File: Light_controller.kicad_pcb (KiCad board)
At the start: 2 copper layers, 11 parts, among them U1 LM358DR, U2 PT8211-S, U3 STM8S003F3P, U4 LTV-356T, U5 LTV-356T

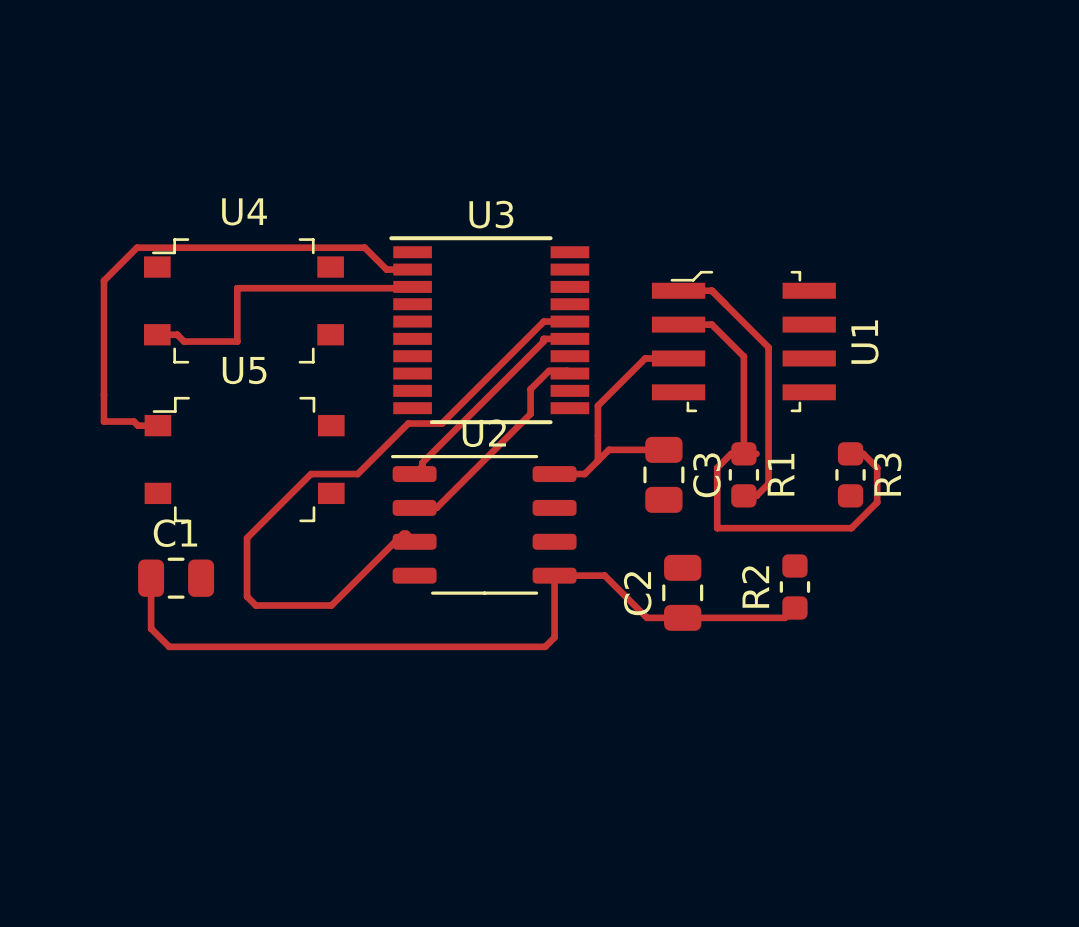
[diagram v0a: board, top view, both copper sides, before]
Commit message: added all circuit except temperature sensor
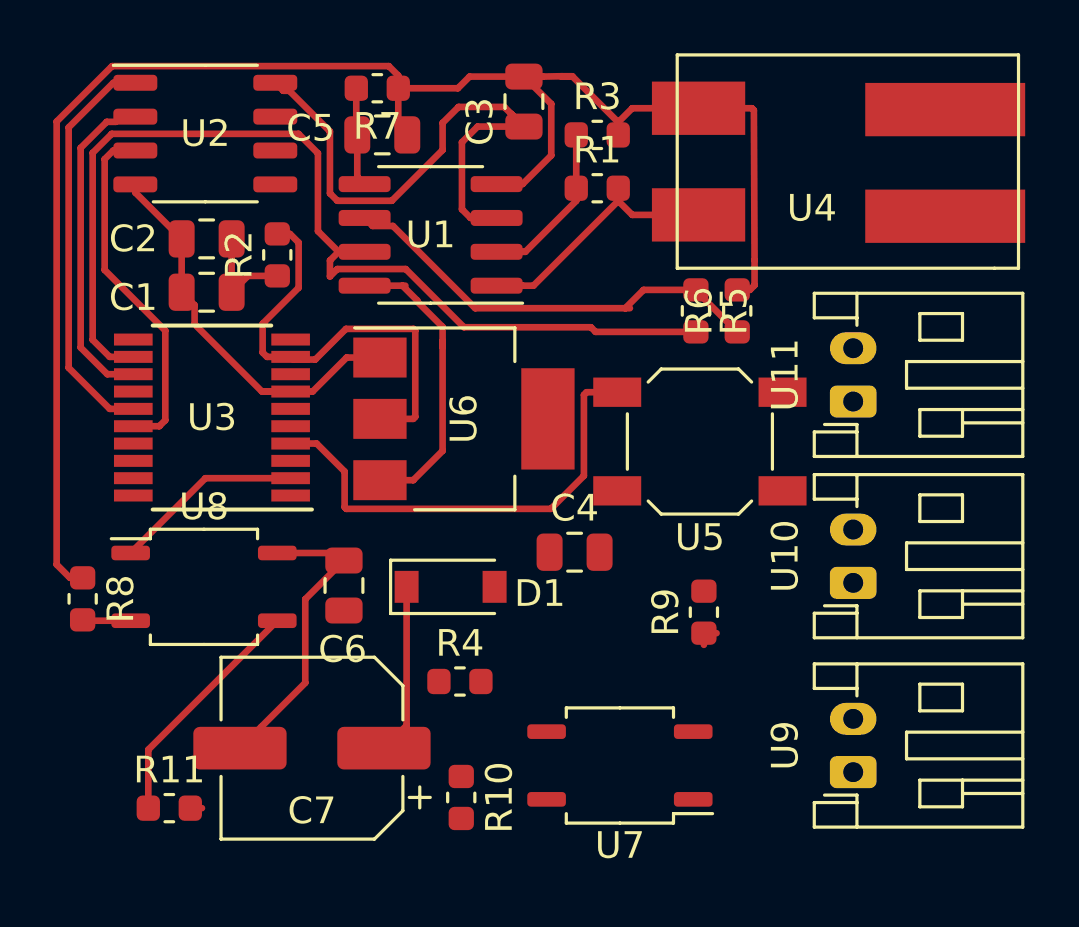
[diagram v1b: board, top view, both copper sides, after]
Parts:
- added C4: C, Capacitor_SMD:C_0805_2012Metric, F.Cu at (170.7, 70.9)
- added C5: C, Capacitor_SMD:C_0805_2012Metric, F.Cu at (163.4, 55.2)
- added C6: C, Capacitor_SMD:C_0805_2012Metric, F.Cu at (162.0, 72.2)
- added C7: 470uF, Capacitor_SMD:CP_Elec_6.3x7.7, F.Cu at (160.8, 78.2)
- added D1: 1N5819HW, Diode_SMD:D_SOD-123, F.Cu at (166.0, 72.2)
- added R10: R, Resistor_SMD:R_0603_1608Metric, F.Cu at (166.4, 80.1)
- added R11: 1K, Resistor_SMD:R_0603_1608Metric, F.Cu at (155.4, 80.5)
- added R4: R, Resistor_SMD:R_0603_1608Metric, F.Cu at (166.3, 75.8)
- added R5: R, Resistor_SMD:R_0603_1608Metric, F.Cu at (175.2, 61.9)
- added R6: R, Resistor_SMD:R_0603_1608Metric, F.Cu at (176.8, 61.9)
- added R7: 0.01Ω, Resistor_SMD:R_0603_1608Metric, F.Cu at (163.2, 53.5)
- added R8: R, Resistor_SMD:R_0603_1608Metric, F.Cu at (152.2, 72.7)
- added R9: R, Resistor_SMD:R_0603_1608Metric, F.Cu at (175.5, 73.2)
- added U10: PH2.0_horizontal, Connector_JST:JST_PH_S2B-PH-K_1x02_P2.00mm_Horizontal, F.Cu at (181.1, 72.0)
- added U11: PH2.0_horizontal, Connector_JST:JST_PH_S2B-PH-K_1x02_P2.00mm_Horizontal, F.Cu at (181.1, 65.2)
- added U6: AMS1117-5.0, Package_TO_SOT_SMD:SOT-223, F.Cu at (166.5, 65.9)
- added U7: EL357N-C, Package_SO:SOP-4_3.8x4.1mm_P2.54mm, F.Cu at (172.3, 78.9)
- added U8: EL357N-C, Package_SO:SOP-4_3.8x4.1mm_P2.54mm, F.Cu at (156.8, 72.2)
- added U9: PH2.0_horizontal, Connector_JST:JST_PH_S2B-PH-K_1x02_P2.00mm_Horizontal, F.Cu at (181.1, 79.2)
- R1, R2, R3: footprint Capacitor_SMD:C_0603_1608Metric -> Resistor_SMD:R_0603_1608Metric
- U1: value LM358DR -> LM358; footprint digikey-footprints:SOIC-8_W3.9mm -> Package_SO:SOIC-8_3.9x4.9mm_P1.27mm
- U4: value LTV-356T -> SMD_2062; footprint digikey-footprints:SMD-4_4.4x3.85mm_P2.54mm -> Custom_footprint_lib:LEDSMD2062
- U5: value LTV-356T -> tact_sw; footprint digikey-footprints:SMD-4_4.4x3.85mm_P2.54mm -> Button_Switch_SMD:SW_SPST_SKQG_WithStem
- moved U4 24.3 mm to (182.5, 62.2), turned to 180 degrees
- moved R2 23.1 mm to (159.5, 59.8)
- moved C2 22.2 mm to (156.8, 59.1), turned to 180 degrees
- moved U2 18.0 mm to (156.8, 55.2)
- moved U5 17.1 mm to (175.3, 66.8), turned to 180 degrees
- moved R3 15.9 mm to (171.5, 55.2), turned to 0 degrees
- moved C3 15.0 mm to (168.8, 54.0), turned to 90 degrees
- moved U1 12.4 mm to (165.2, 59.0), turned to 180 degrees
- moved R1 12.1 mm to (171.5, 57.2), turned to 0 degrees
- moved U3 11.0 mm to (157.1, 65.8), turned to 180 degrees
- moved C1 10.8 mm to (156.8, 61.1), turned to 180 degrees
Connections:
- net Net-(U3-Pad10) renamed /PA3
- net Net-(U3-Pad11) renamed /PB5
- net Net-(U3-Pad14) renamed /PC4
- net Net-(U3-Pad17) renamed /PC7
- net Net-(U3-Pad19) renamed /PD2
- net Net-(U3-Pad20) renamed /V_SENSOR
- net Net-(U3-Pad5) renamed /PA1
- net Net-(U3-Pad6) renamed /PA2
- net Net-(U3-Pad8) renamed /VCAP
- U1 pad 5: (no net) -> /CURRENT_IN
- U1 pad 6: (no net) -> Net-(R5-Pad1)
- U1 pad 7: (no net) -> /C_SENSOR
- U2 pad 6: (no net) -> Net-(U2-Pad6)
- U3 pad 12: Net-(U3-Pad12) -> /C_SENSOR
- U3 pad 4: /SWIM_RST -> /RESET
- U3 pad 9: Net-(U3-Pad9) -> /5V_SUPPLY
- U4 pad 1: Net-(U4-Pad1) -> Net-(R1-Pad2)
- U4 pad 2: /UART_RX -> GND
- U5 pad 1: /UART_TX -> GND
- U5 pad 2: GND -> /RESET
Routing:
- net GND: track 0.00 -> 78.5 mm
- net /C_SENSOR: track 0.00 -> 39.2 mm
- net Net-(C1-Pad1): track 29.6 -> 3.97 mm
- net /RESET: track 0.00 -> 17.6 mm
- net /5V_SUPPLY: track 0.00 -> 16.8 mm
- net Net-(R5-Pad1): track 0.00 -> 16.5 mm
- net Net-(R1-Pad1): track 19.5 -> 6.25 mm
- net /UART_TX: track 19.8 -> 7.16 mm
- net /SPI_MOSI: track 25.3 -> 13.3 mm
- net /RCH: track 10.3 -> 22.1 mm
- net +12V: track 0.00 -> 11.4 mm
- net Net-(C6-Pad1): track 0.00 -> 11.3 mm
- net /UART_RX: track 11.7 -> 0.91 mm
- net Net-(R11-Pad1): track 0.00 -> 9.03 mm
- net /SPI_SCK: track 8.05 -> 15.3 mm
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
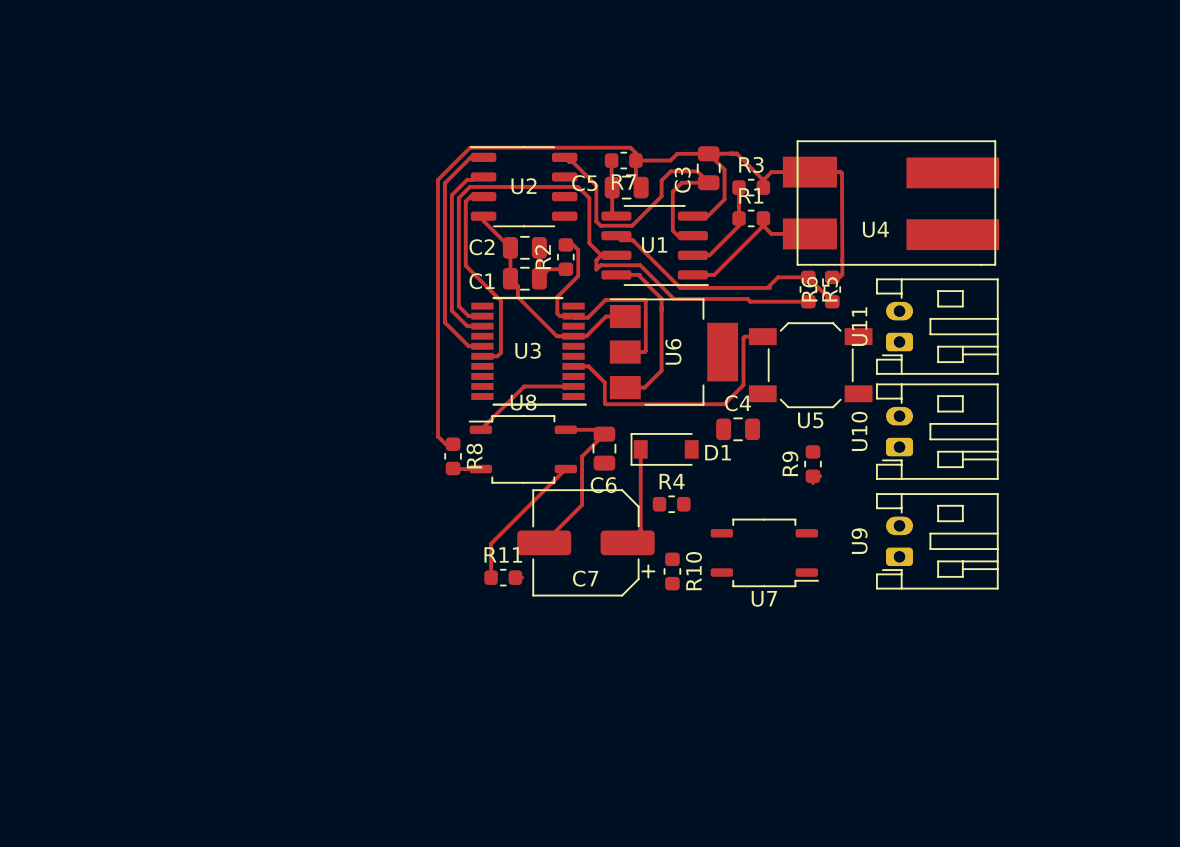
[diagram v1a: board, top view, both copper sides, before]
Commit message: modified ph2.0 to smd , changed thermistor to a ph2.0 and rerouted the layout again with via
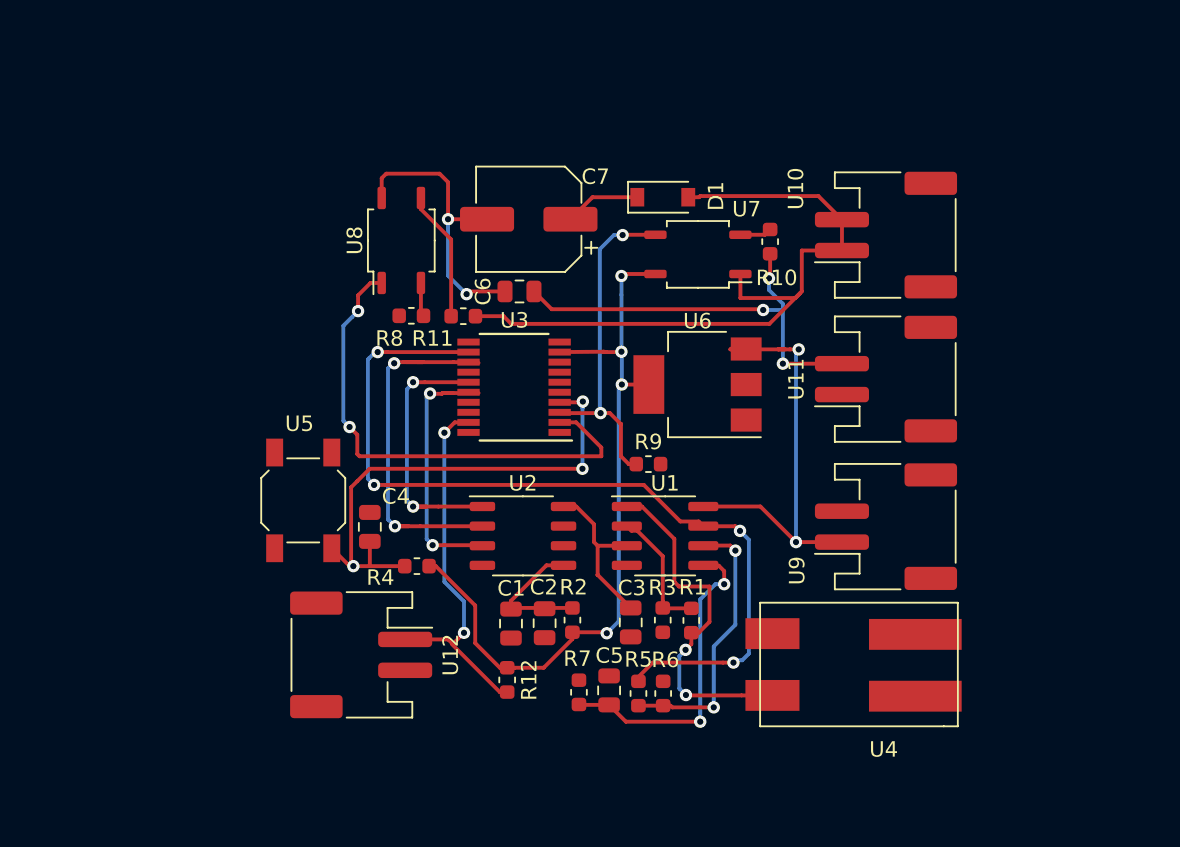
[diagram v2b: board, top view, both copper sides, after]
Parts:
- added R12: R, Resistor_SMD:R_0603_1608Metric, F.Cu at (155.7, 87.1)
- added U12: PH2.0_horizontal, Connector_JST:JST_PH_S2B-PH-SM4-TB_1x02-1MP_P2.00mm_Horizontal, F.Cu at (146.2, 85.5)
- U10, U11, U9: footprint Connector_JST:JST_PH_S2B-PH-K_1x02_P2.00mm_Horizontal -> Connector_JST:JST_PH_S2B-PH-SM4-TB_1x02-1MP_P2.00mm_Horizontal
- U6: footprint Package_TO_SOT_SMD:SOT-223 -> Package_TO_SOT_SMD:SOT-223-3_TabPin2
- moved R7 34.5 mm to (160.3, 87.9), turned to 270 degrees
- moved U5 34.0 mm to (142.5, 75.5), turned to 90 degrees
- moved C5 32.6 mm to (162.3, 87.8), turned to 90 degrees
- moved U4 30.0 mm to (180.1, 92.1)
- moved C3 29.8 mm to (163.7, 83.4), turned to 270 degrees
- moved R3 28.6 mm to (165.8, 83.2), turned to 270 degrees
- moved R5 28.4 mm to (164.2, 88.0), turned to 90 degrees
- moved R6 28.4 mm to (165.8, 88.0)
- moved R1 26.3 mm to (167.6, 83.3), turned to 270 degrees
- moved C4 24.7 mm to (146.8, 77.2), turned to 90 degrees
- moved C2 24.3 mm to (158.1, 83.5), turned to 270 degrees
- moved R2 23.5 mm to (159.9, 83.2), turned to 270 degrees
- moved U2 22.6 mm to (156.7, 77.8)
- moved C1 22.3 mm to (155.9, 83.5), turned to 270 degrees
- moved R10 22.3 mm to (172.7, 58.8)
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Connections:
- U1 pad 8: +12V -> /12V_INPUT
- U3 pad 19: /PD2 -> /TEMP_SENSOR
- U6 pad 3: +12V -> /12V_INPUT
- U9 pad 1: /12V_EXT -> /12V_INPUT
- U9 pad 2: /EXT_GND -> GND
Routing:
- net GND: track 78.5 -> 0.00 mm
- net /RX_in: track 0.44 -> 45.6 mm
- net /5V_SUPPLY: track 16.8 -> 48.7 mm, vias 0 -> 4
- net /EXT_GND: track 0.00 -> 29.2 mm, vias 0 -> 3
- net /12V_INPUT: track 0.00 -> 27.4 mm, vias 0 -> 2
- net /UART_TX: track 7.16 -> 32.7 mm, vias 0 -> 2
- net /TEMP_SENSOR: track 0.00 -> 24.4 mm, vias 0 -> 2
- net /UART_RX: track 0.91 -> 22.2 mm, vias 0 -> 2
- net /C_SENSOR: track 39.2 -> 56.1 mm, vias 0 -> 4
- net /CURRENT_IN: track 4.17 -> 20.6 mm, vias 0 -> 2
- net /RESET: track 17.6 -> 33.3 mm, vias 0 -> 3
- net Net-(R1-Pad2): track 9.58 -> 22.6 mm, vias 0 -> 2
- net /WS: track 12.4 -> 24.5 mm, vias 0 -> 2
- net +12V: track 11.4 -> 0.00 mm
- net /RCH: track 22.1 -> 10.8 mm
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
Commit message: modified layout but havent fill ground yet
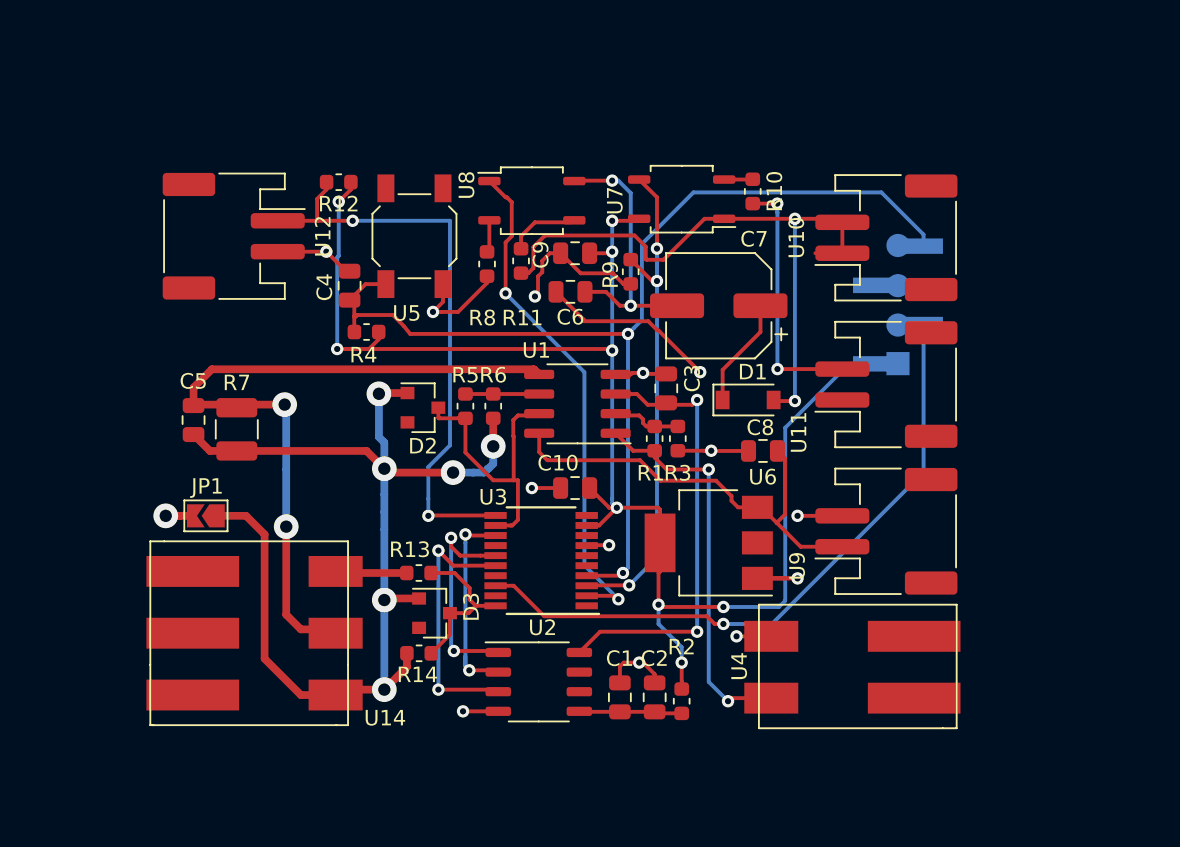
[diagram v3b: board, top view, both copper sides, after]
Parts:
- added C10: C, Capacitor_SMD:C_0805_2012Metric, F.Cu at (160.1, 74.7)
- added C8: C, Capacitor_SMD:C_0805_2012Metric, F.Cu at (172.3, 72.3)
- added C9: C, Capacitor_SMD:C_0805_2012Metric, F.Cu at (160.1, 59.5)
- added D2: BZX84Cxx, Diode_SMD:D_SOT-23_ANK, F.Cu at (150.2, 69.5)
- added D3: BZX84Cxx, Diode_SMD:D_SOT-23_ANK, F.Cu at (151.0, 82.8)
- added JP1: SolderJumper_2_Open, Jumper:SolderJumper-2_P1.3mm_Open_TrianglePad1.0x1.5mm, F.Cu at (136.2, 76.5)
- added R13: R, Resistor_SMD:R_0603_1608Metric, F.Cu at (150.0, 80.2)
- added R14: R, Resistor_SMD:R_0603_1608Metric, F.Cu at (150.0, 85.4)
- added U13: PinSocket_1x4, Custom_footprint_lib:custom_pinsocket_1x04_p2.54, B.Cu at (181.0, 72.2)
- added U14: SMD2063, Custom_footprint_lib:SMD2063, F.Cu at (136.8, 74.0)
- R7: footprint Resistor_SMD:R_0603_1608Metric -> Resistor_SMD:R_1210_3225Metric
- moved R12 34.0 mm to (144.8, 54.9), turned to 180 degrees
- moved C5 32.1 mm to (135.4, 70.3), turned to 270 degrees
- moved U12 28.3 mm to (138.0, 58.4)
- moved R7 27.9 mm to (138.2, 70.9), turned to 90 degrees
- moved R5 21.7 mm to (153.0, 69.4), turned to 270 degrees
- moved R6 21.6 mm to (154.8, 69.4), turned to 270 degrees
- moved U5 18.6 mm to (149.7, 58.4), turned to 270 degrees
- moved C4 15.7 mm to (145.5, 61.6)
- moved R4 15.5 mm to (146.6, 64.6)
- moved C3 15.3 mm to (166.0, 68.2), turned to 90 degrees
- moved D1 14.2 mm to (171.3, 69.0)
- moved C7 13.5 mm to (169.4, 62.9)
- moved R9 12.5 mm to (163.7, 60.7), turned to 270 degrees
- moved R1 12.0 mm to (165.2, 71.5)
- moved R3 11.8 mm to (166.8, 71.5)
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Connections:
- net /CURRENT_IN renamed /LED_SENSE
- net /PA1 renamed Net-(U3-Pad5)
- net /PA2 renamed Net-(U3-Pad6)
- net /PA3 renamed Net-(U3-Pad10)
- net /PC4 renamed Net-(U3-Pad14)
- net /PC7 renamed Net-(U3-Pad17)
- net /UART_CLOCK renamed Net-(U3-Pad1)
- net /VCAP renamed Net-(U3-Pad8)
- C5 pad 2: GND -> /LED-
- R6 pad 2: GND -> /LED-
- R7 pad 1: GND -> /LED-
- U3 pad 11: /PB5 -> /TEMP_SENSOR
- U3 pad 19: /TEMP_SENSOR -> Net-(U3-Pad19)
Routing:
- net /LED-: track 0.00 -> 70.5 mm, vias 0 -> 6
- net /5V_SUPPLY: track 48.7 -> 101.7 mm, vias 4 -> 9
- net GND: track 0.00 -> 50.8 mm, vias 0 -> 13
- net /SWIM: track 0.00 -> 42.4 mm, vias 0 -> 1
- net /C_SENSOR: track 56.1 -> 19.2 mm, vias 4 -> 0
- net /RESET: track 33.3 -> 69.5 mm, vias 3 -> 2
- net /LED_SENSE: track 20.6 -> 46.7 mm
- net /RCH: track 10.8 -> 28.9 mm, vias 0 -> 2
- net Net-(R5-Pad1): track 17.9 -> 4.18 mm, vias 2 -> 0
- net /TEMP_SENSOR: track 24.4 -> 37.9 mm
- net /WS: track 24.5 -> 13.5 mm
- net /V_SENSOR: track 0.00 -> 10.9 mm
- net /UART_RX: track 22.2 -> 33.0 mm, vias 2 -> 3
- net /LED+: track 0.00 -> 4.64 mm
- net Net-(R1-Pad1): track 8.34 -> 4.51 mm
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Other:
- net class BIG CURRENT added: clearance 0.4, trace_width 0.5, via_dia 1.6, via_drill 0.8

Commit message: updated the layout
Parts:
- JP1: value SolderJumper_2_Open -> Jumper_2_Open
- moved C5 8.52 mm to (143.8, 71.7), turned to 0 degrees
- moved R7 7.12 mm to (144.4, 74.4), turned to 180 degrees
- moved R13 6.66 mm to (149.1, 86.8)
- moved JP1 6.09 mm to (138.6, 70.9)
- moved R14 4.17 mm to (148.8, 81.4)
- moved D2 2.40 mm to (150.1, 71.9)
- moved R5 2.30 mm to (153.1, 71.7)
- moved R6 2.30 mm to (154.9, 71.7)
- moved D3 2.25 mm to (149.1, 84.0)
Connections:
- U14 pad 1: /LED+ -> /LED-
- U14 pad 3: /LED- -> /LED+
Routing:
- net /LED-: track 70.5 -> 40.9 mm, vias 6 -> 2
- net /LED_SENSE: track 46.7 -> 35.5 mm
- net /EXT_GND: track 28.5 -> 33.2 mm
- net /V_SENSOR: track 10.9 -> 12.9 mm
- net Net-(R5-Pad1): track 4.18 -> 5.89 mm
- net /RESET: track 69.5 -> 71.1 mm
- net /WS: track 13.5 -> 11.9 mm
- net GND: track 50.8 -> 52.2 mm
- net /SWIM: track 42.4 -> 43.4 mm
- net /UART_TX: track 33.1 -> 33.9 mm
- net /RCH: track 28.9 -> 29.7 mm
- net /SPI_MOSI: track 17.4 -> 16.8 mm
